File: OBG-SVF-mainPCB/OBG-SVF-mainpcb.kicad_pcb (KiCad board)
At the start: 2 copper layers, 50.8 x 76.2 mm, 38 parts, among them J7 EURO_PWR_2x5, J8 Conn_02x06_Odd_Even, Q1 2N3904, Q2 2N3906, Q3 2N3906, U1 TL084, U2 LM13700

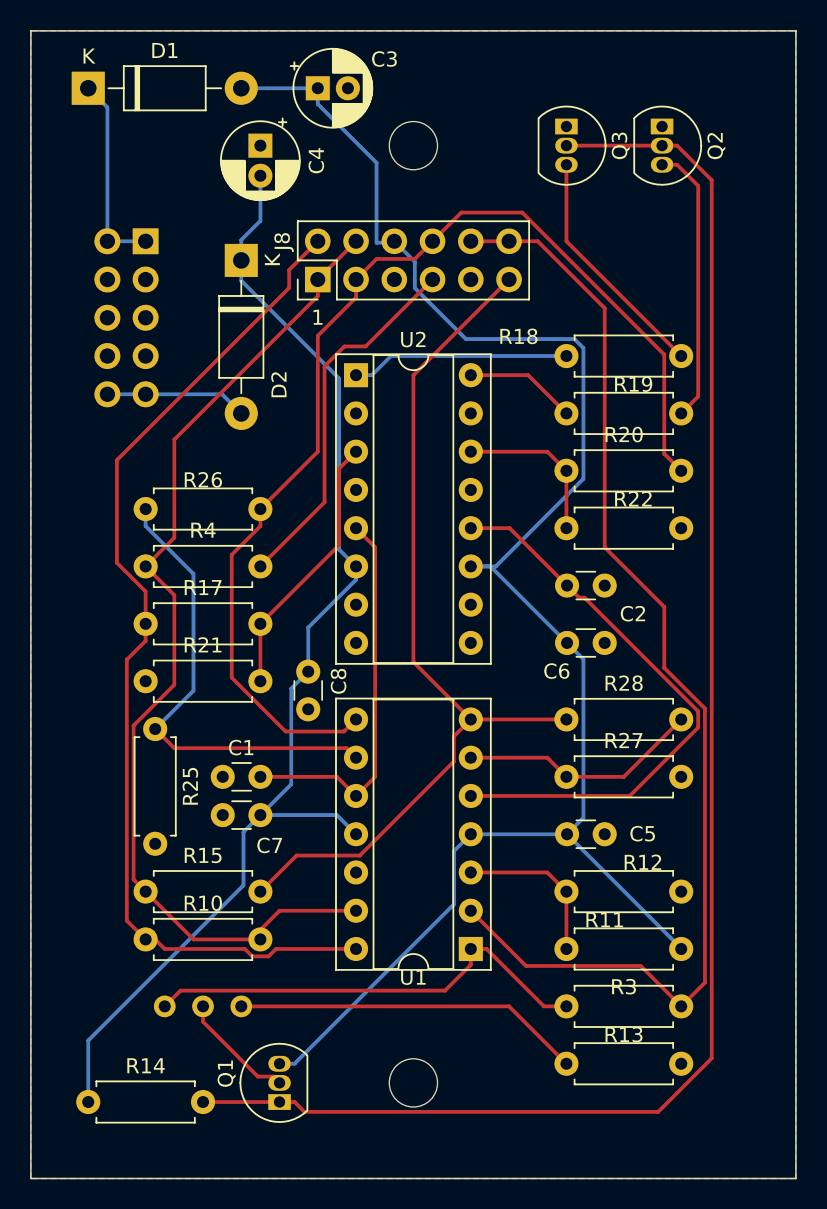
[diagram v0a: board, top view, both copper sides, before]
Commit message: Panel PCB Gerbers, some schematic updates
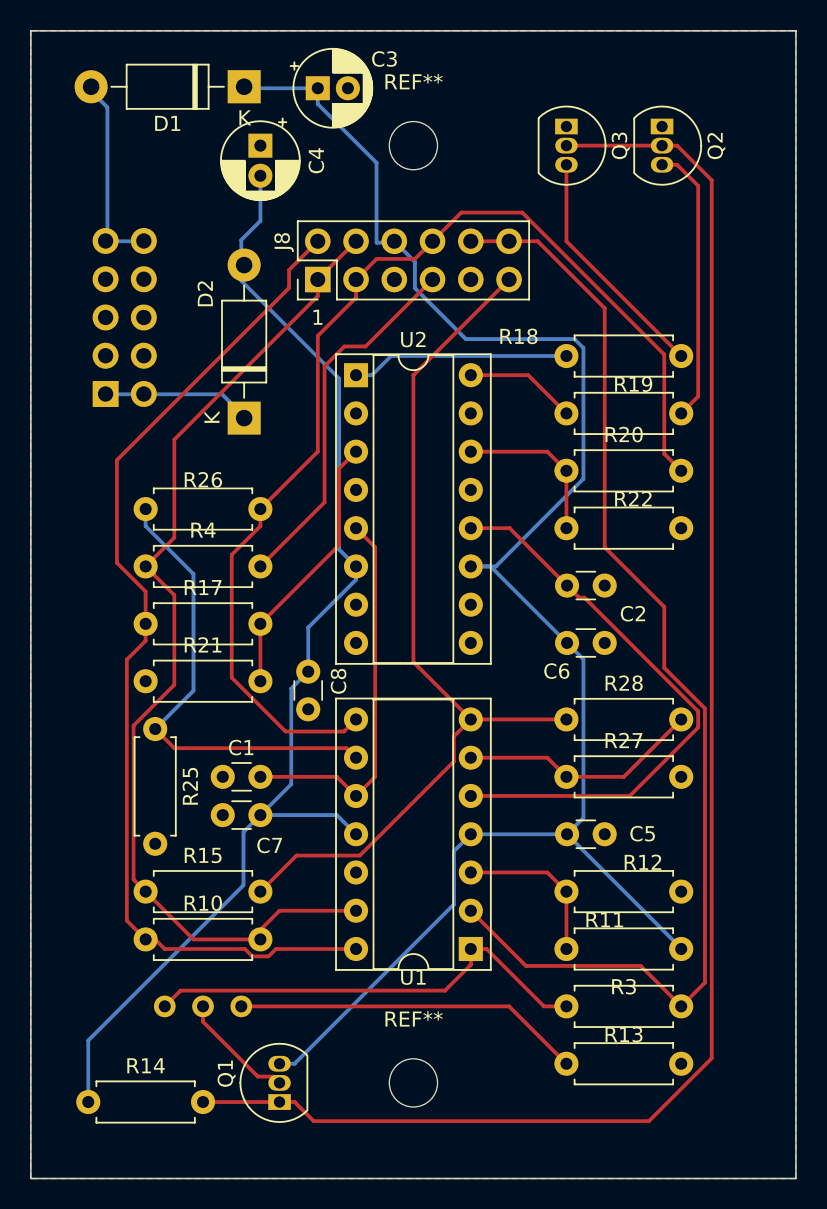
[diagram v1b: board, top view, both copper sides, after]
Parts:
- J7: footprint Connector_IDC:IDC-Header_2x05_P2.54mm_Vertical -> EurorackRSH:Eurorack_Power_Header_Shrouded
- moved J7 10.5 mm to (121.8, 58.4), turned to 0 degrees
- moved D2 10.5 mm to (131.0, 60.0), turned to 90 degrees
- moved D1 10.4 mm to (131.0, 38.0), turned to 180 degrees
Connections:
- D1 pad 1: Net-(D1-Pad1) -> +12V
- D1 pad 2: +12V -> Net-(D1-Pad2)
- D2 pad 1: -12V -> Net-(D2-Pad1)
- D2 pad 2: Net-(D2-Pad2) -> -12V
- J7 pad 1: Net-(D1-Pad1) -> Net-(D2-Pad1)
- J7 pad 10: Net-(D2-Pad2) -> Net-(D1-Pad2)
- J7 pad 2: Net-(D1-Pad1) -> Net-(D2-Pad1)
- J7 pad 9: Net-(D2-Pad2) -> Net-(D1-Pad2)
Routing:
- net Net-(D1-Pad2): track 0.00 -> 13.2 mm
- net Net-(D1-Pad1): track 13.2 -> 0.00 mm
- net Net-(D2-Pad2): track 9.42 -> 0.00 mm
- net Net-(D2-Pad1): track 0.00 -> 9.42 mm
- net /VC: track 104.4 -> 104.9 mm
